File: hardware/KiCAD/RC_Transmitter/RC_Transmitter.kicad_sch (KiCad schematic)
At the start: 9 parts, among them SW1 SW_Push, SW2 SW_Push, U1 NRF24L01_Breakout

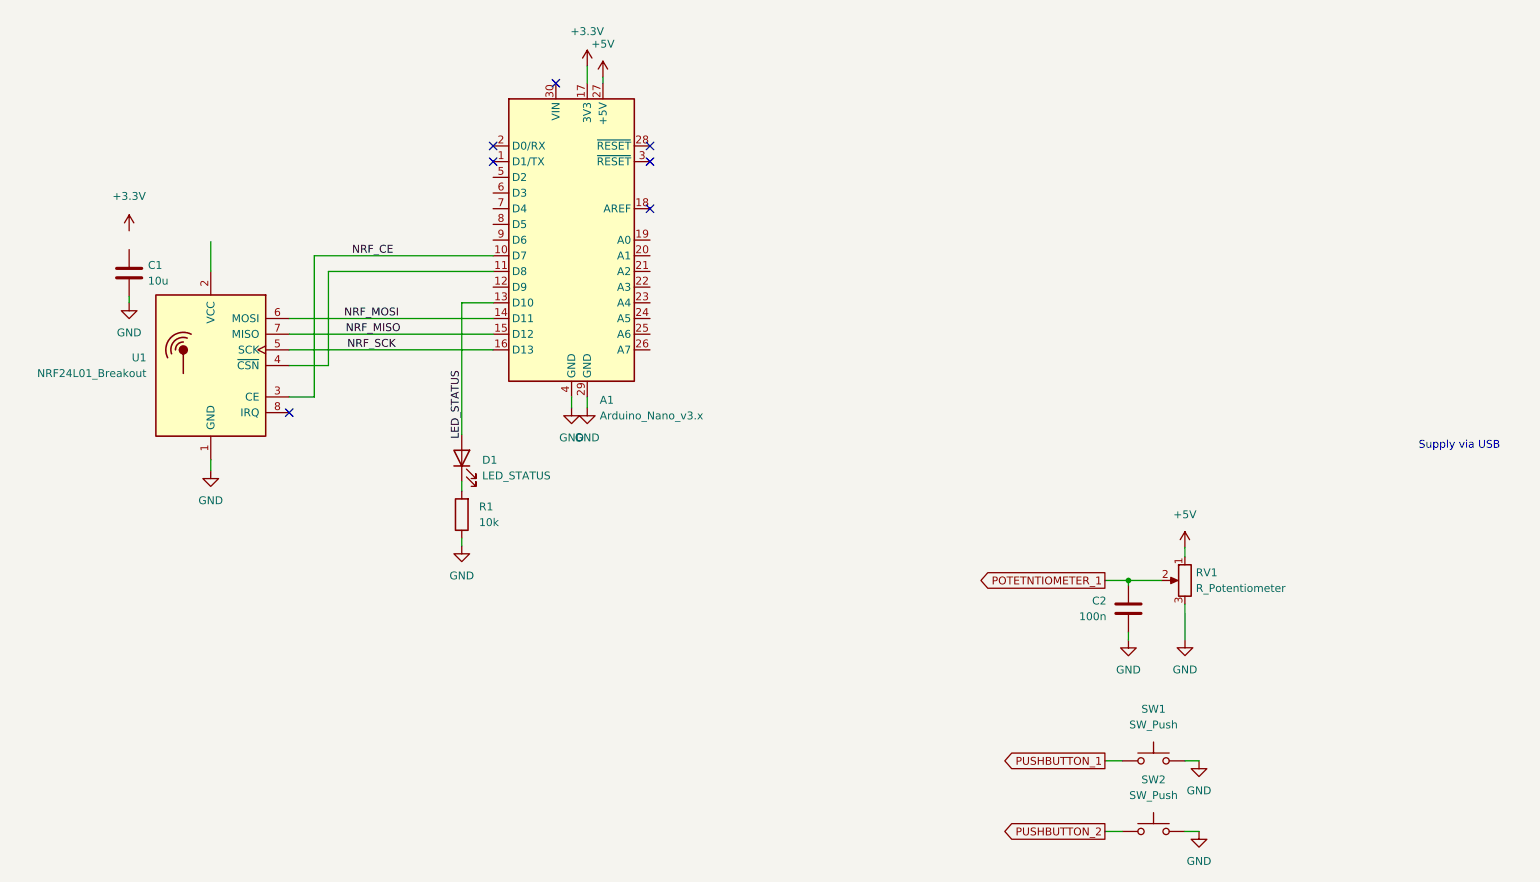
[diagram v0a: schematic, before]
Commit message: add schematic net names like described in the readme
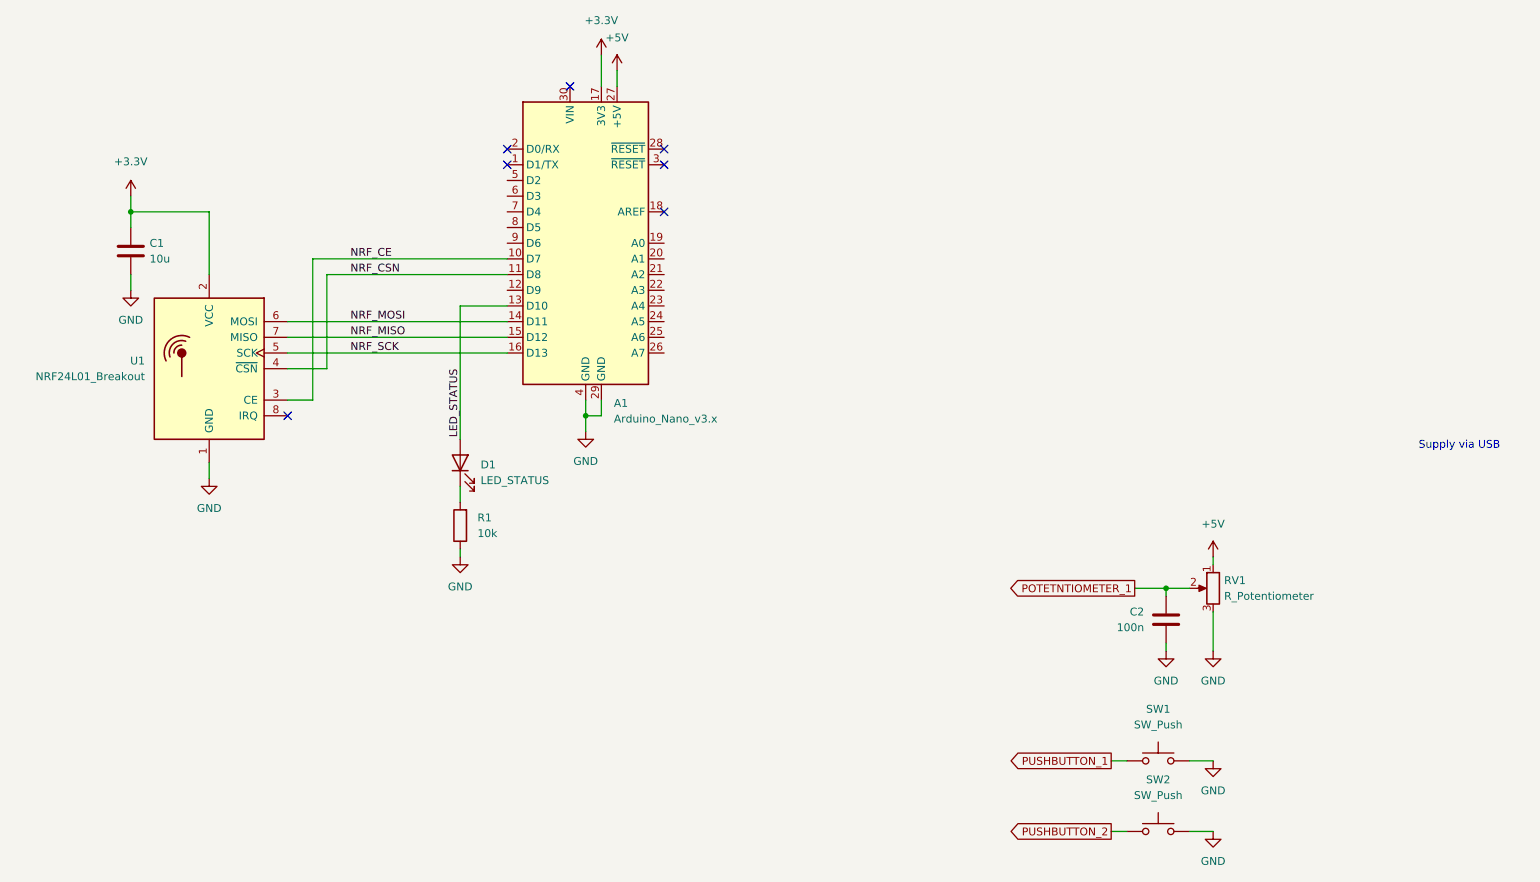
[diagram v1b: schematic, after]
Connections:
- net +3V3: now also C1.1, U1.2 (VCC)
- net NRF_CSN: now reaches A1.11 (D8), U1.4 (~{CSN})
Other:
- moved on the sheet: A1, C1, C2, D1, R1, RV1, SW1, SW2, U1

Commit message: connect HMI (Button & Poti) to MCU
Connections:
- net POTETNTIOMETER_1 is gone; now on net POTI_1: C2.1, RV1.2
- net PUSHBUTTON_1: now also A1.5 (D2)
- net PUSHBUTTON_2: now also A1.6 (D3)
- net POTI_1: now reaches A1.19 (A0)
- no-connect marks 7 -> 18
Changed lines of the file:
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@@
   (junction (at 106.68 86.36) (diameter 0) (color 0 0 0 0)
   )
+  (no_connect (at 93.98 66.04))
+  (no_connect (at 93.98 53.34))
+  (no_connect (at 93.98 55.88))
+  (no_connect (at 93.98 58.42))
+  (no_connect (at 119.38 60.96))
+  (no_connect (at 119.38 63.5))
+  (no_connect (at 119.38 66.04))
+  (no_connect (at 119.38 68.58))
+  (no_connect (at 119.38 71.12))
+  (no_connect (at 119.38 73.66))
+  (no_connect (at 119.38 76.2))
   (no_connect (at 104.14 33.02))
   (no_connect (at 93.98 43.18))
@@
     (stroke (width 0) (type default) (color 0 0 0 0))
   )
+  (wire (pts (xy 119.38 58.42) (xy 123.19 58.42))
+    (stroke (width 0) (type default) (color 0 0 0 0))
+  )
   (wire (pts (xy 58.42 76.2) (xy 93.98 76.2))
     (stroke (width 0) (type default) (color 0 0 0 0))
@@
     (stroke (width 0) (type default) (color 0 0 0 0))
   )
+  (wire (pts (xy 91.44 48.26) (xy 93.98 48.26))
+    (stroke (width 0) (type default) (color 0 0 0 0))
+  )
   (wire (pts (xy 64.77 63.5) (xy 93.98 63.5))
     (stroke (width 0) (type default) (color 0 0 0 0))
@@
     (stroke (width 0) (type default) (color 0 0 0 0))
   )
+  (wire (pts (xy 91.44 50.8) (xy 93.98 50.8))
+    (stroke (width 0) (type default) (color 0 0 0 0))
+  )
   (wire (pts (xy 106.68 86.36) (xy 106.68 88.9))
     (stroke (width 0) (type default) (color 0 0 0 0))
@@
     )
   )
-  (global_label "POTETNTIOMETER_1" (shape output) (at 195.58 114.3 180) (fields_autoplaced)
+  (global_label "POTI_1" (shape output) (at 195.58 114.3 180) (fields_autoplaced)
+    (effects (font (size 1.27 1.27)) (justify right))
+    (property "Intersheet References" "${INTERSHEET_REFS}" (id 0) (at 186.8169 114.2206 0)
+      (effects (font (size 1.27 1.27)) (justify right) hide)
+    )
+  )
+  (global_label "PUSHBUTTON_1" (shape input) (at 91.44 48.26 180) (fields_autoplaced)
     (effects (font (size 1.27 1.27)) (justify right))
-    (property "Intersheet References" "${INTERSHEET_REFS}" (id 0) (at 175.0845 114.2206 0)
+    (property "Intersheet References" "${INTERSHEET_REFS}" (id 0) (at 74.5126 48.1806 0)
       (effects (font (size 1.27 1.27)) (justify right) hide)
     )
   )
+  (global_label "POTI_1" (shape input) (at 123.19 58.42 0) (fields_autoplaced)
+    (effects (font (size 1.27 1.27)) (justify left))
+    (property "Intersheet References" "${INTERSHEET_REFS}" (id 0) (at 131.9531 58.4994 0)
+      (effects (font (size 1.27 1.27)) (justify left) hide)
+    )
+  )
   (global_label "PUSHBUTTON_2" (shape output) (at 191.77 153.67 180) (fields_autoplaced)
     (effects (font (size 1.27 1.27)) (justify right))
@@
       (effects (font (size 1.27 1.27)) (justify right) hide)
     )
+  )
+  (global_label "PUSHBUTTON_2" (shape input) (at 91.44 50.8 180) (fields_autoplaced)
+    (effects (font (size 1.27 1.27)) (justify right))
+    (property "Intersheet References" "${INTERSHEET_REFS}" (id 0) (at 74.5126 50.7206 0)
+      (effects (font (size 1.27 1.27)) (justify right) hide)
+    )

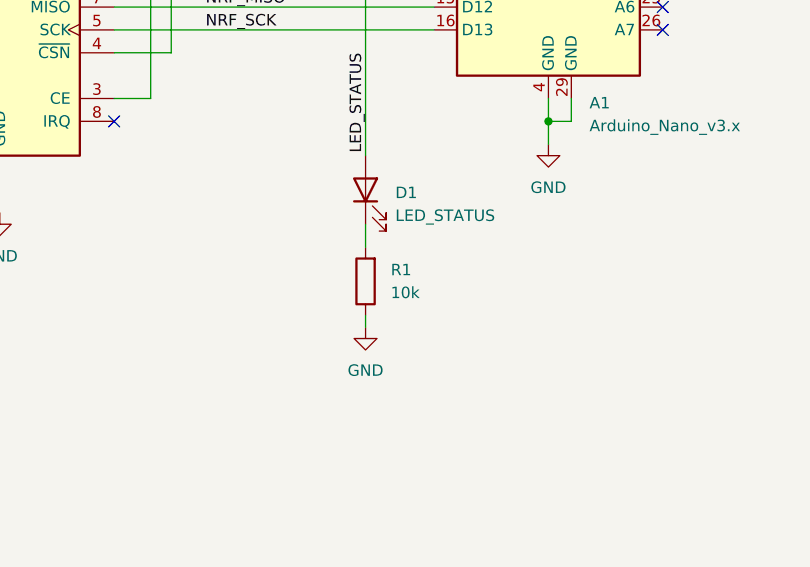
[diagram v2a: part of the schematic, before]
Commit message: change value of series resistor for status LED
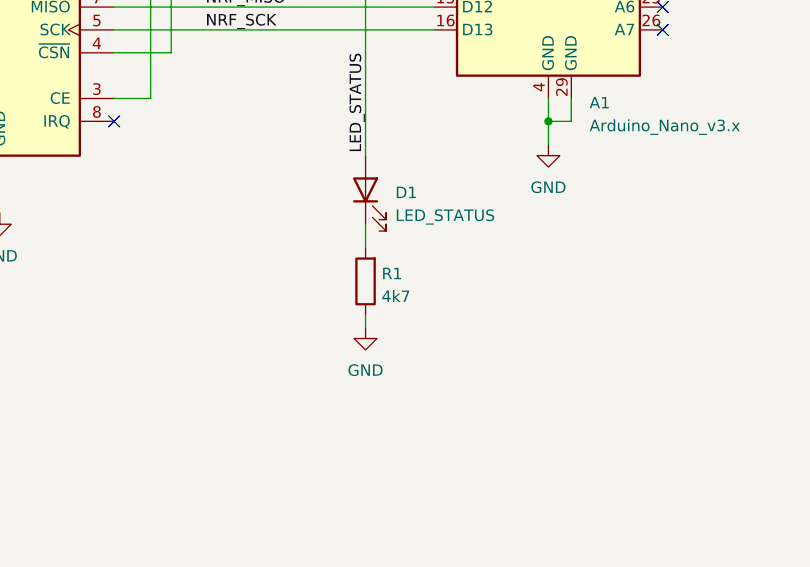
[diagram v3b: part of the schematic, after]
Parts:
- R1: value 10k -> 4k7
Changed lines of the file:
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@@
   (symbol (lib_id "Device:R") (at 86.36 104.14 180) (unit 1)
     (in_bom yes) (on_board yes) (fields_autoplaced)
-    (property "Reference" "R1" (id 0) (at 89.154 102.8699 0)
+    (property "Reference" "R1" (id 0) (at 88.138 103.3053 0)
       (effects (font (size 1.27 1.27)) (justify right))
     )
-    (property "Value" "10k" (id 1) (at 89.154 105.4099 0)
+    (property "Value" "4k7" (id 1) (at 88.138 105.8422 0)
       (effects (font (size 1.27 1.27)) (justify right))
     )
@@
     )
     (path "/710c87df-58cf-4d1c-ad64-932a210b6aae"
-      (reference "R1") (unit 1) (value "10k") (footprint "")
+      (reference "R1") (unit 1) (value "4k7") (footprint "")
     )
     (path "/21baf089-0668-4767-b44b-1272d0a61348"
